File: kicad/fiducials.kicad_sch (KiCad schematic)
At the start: 4 parts

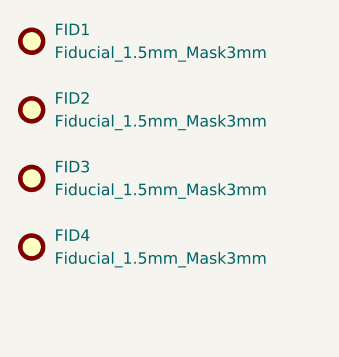
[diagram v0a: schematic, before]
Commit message: add: another one fiducial
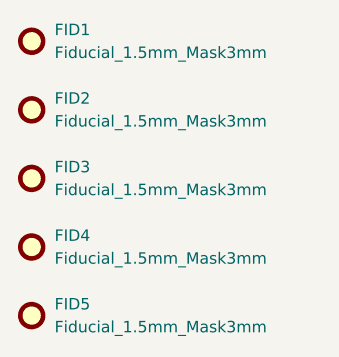
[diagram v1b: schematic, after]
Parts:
- added FID5: Fiducial_1.5mm_Mask3mm, Fiducial:Fiducial_1.5mm_Mask3mm, symbol Mechanical:Fiducial
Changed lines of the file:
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@@
+    )
+  )
+  (symbol (lib_id "Mechanical:Fiducial") (at 144.78 124.46 0) (unit 1)
+    (in_bom yes) (on_board yes) (dnp no) (fields_autoplaced)
+    (property "Reference" "FID5" (at 147.32 123.19 0)
+      (effects (font (size 1.27 1.27)) (justify left))
+    )
+    (property "Value" "Fiducial_1.5mm_Mask3mm" (at 147.32 125.73 0)
+      (effects (font (size 1.27 1.27)) (justify left))
+    )
+    (property "Footprint" "Fiducial:Fiducial_1.5mm_Mask3mm" (at 144.78 124.46 0)
+      (effects (font (size 1.27 1.27)) hide)
+    )
+    (property "Datasheet" "~" (at 144.78 124.46 0)
+      (effects (font (size 1.27 1.27)) hide)
+    )
+    (instances
+      (project "RadioSens"
+        (path "/d8a72df0-904a-413a-8147-12e635dec35e/94dee1d1-e75f-474e-a2d5-3d7d7eb2659b"
+          (reference "FID5") (unit 1)
+        )
+      )
     )
   )
